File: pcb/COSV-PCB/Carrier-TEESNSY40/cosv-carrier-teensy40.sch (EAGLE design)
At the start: 21 parts, among them K1 61200821621, K2 61200821621, K3 61200821621

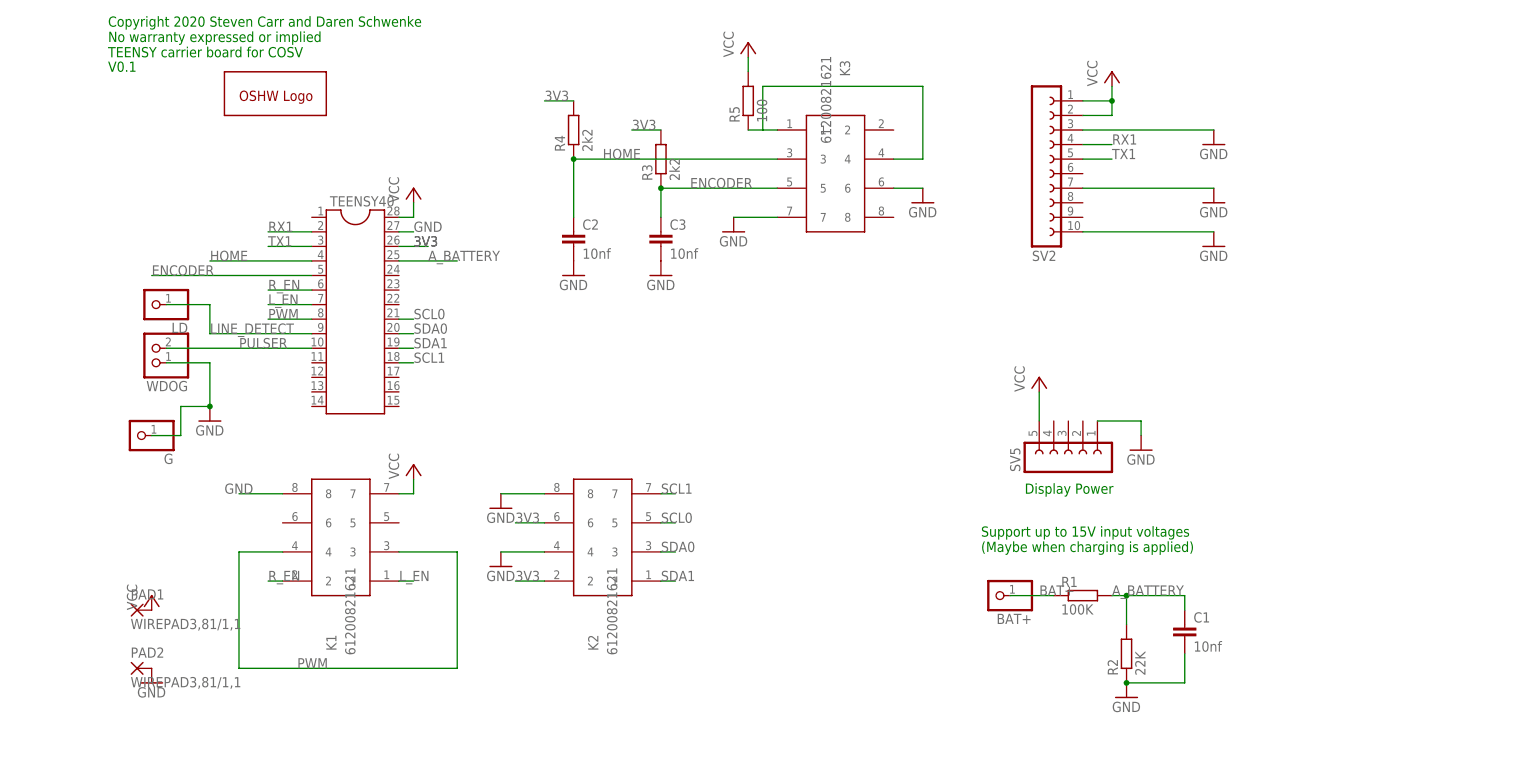
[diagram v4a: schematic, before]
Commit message: Update millable COSV carrier PCB to support milling with a dremel spindle This adds a few more jumpers, but it eliminates the tiny traces between pins that plague milling a board with a dremel spindle.
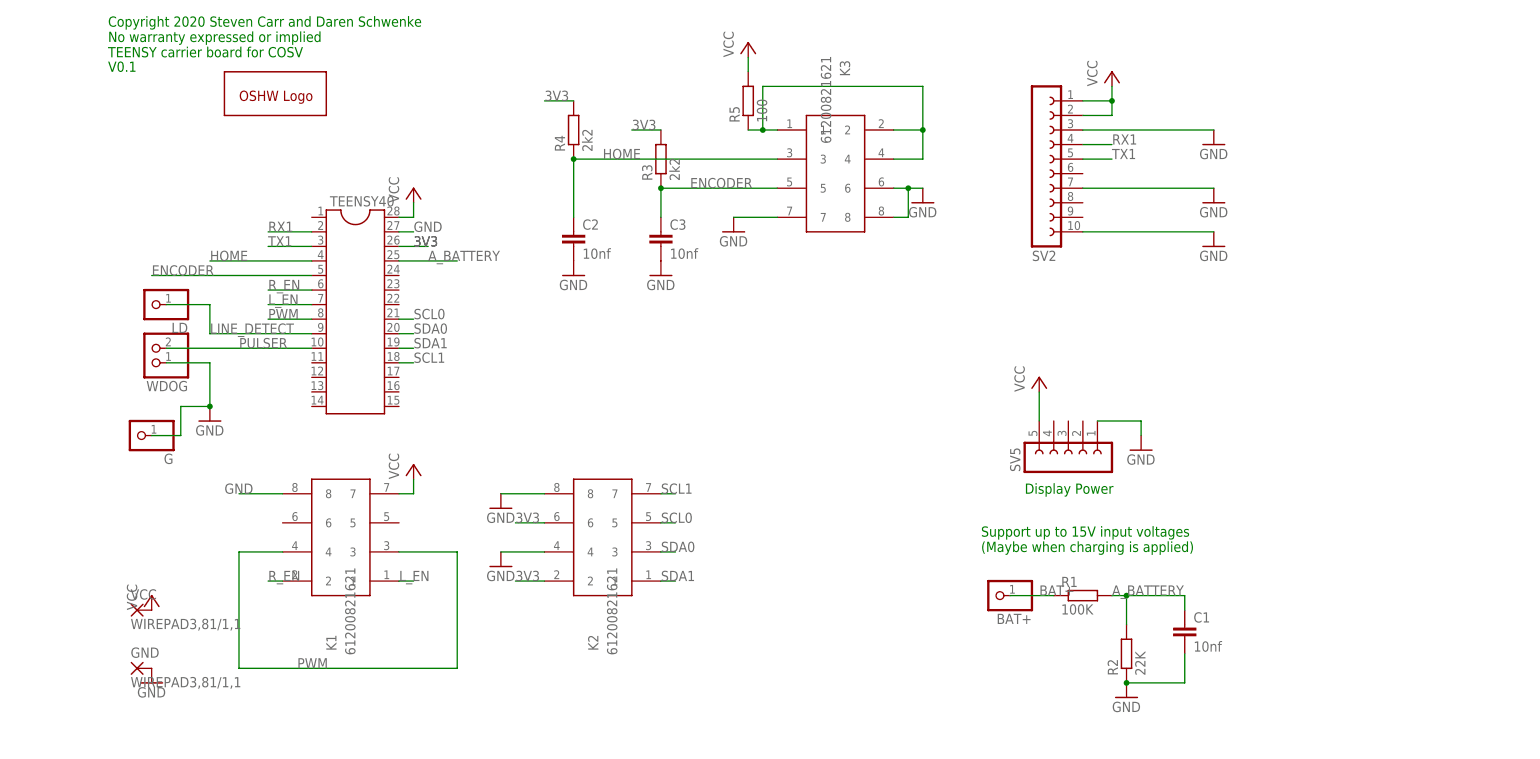
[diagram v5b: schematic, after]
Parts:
- renumbered PAD1 to VCC, PAD2 to GND
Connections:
- net GND: now also K3.8
- net N$1: now also K3.2
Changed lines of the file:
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@@
 <part name="GND3" library="supply1" deviceset="GND" device=""/>
 <part name="K3" library="Wuerth_Elektronik_eiCan_05_Box_Header_IDC_Connectors_1_2" deviceset="61200821621" device=""/>
-<part name="PAD1" library="wirepad" deviceset="WIREPAD" device="3,81/1,1"/>
-<part name="PAD2" library="wirepad" deviceset="WIREPAD" device="3,81/1,1"/>
+<part name="VCC" library="wirepad" deviceset="WIREPAD" device="3,81/1,1"/>
+<part name="GND" library="wirepad" deviceset="WIREPAD" device="3,81/1,1"/>
 <part name="P+1" library="supply1" deviceset="VCC" device=""/>
 <part name="GND1" library="supply1" deviceset="GND" device=""/>
@@
 <instance part="GND3" gate="1" x="71.12" y="25.4"/>
 <instance part="K3" gate="G$1" x="129.54" y="96.52" rot="R270"/>
-<instance part="PAD1" gate="G$1" x="7.62" y="17.78"/>
-<instance part="PAD2" gate="G$1" x="7.62" y="7.62"/>
+<instance part="VCC" gate="G$1" x="7.62" y="17.78"/>
+<instance part="GND" gate="G$1" x="7.62" y="7.62"/>
 <instance part="P+1" gate="VCC" x="10.16" y="20.32"/>
 <instance part="GND1" gate="1" x="10.16" y="5.08"/>
@@
 </segment>
 <segment>
-<pinref part="PAD1" gate="G$1" pin="P"/>
+<pinref part="VCC" gate="G$1" pin="P"/>
 <pinref part="P+1" gate="VCC" pin="VCC"/>
 </segment>
@@
 </segment>
 <segment>
-<pinref part="PAD2" gate="G$1" pin="P"/>
+<pinref part="GND" gate="G$1" pin="P"/>
 <pinref part="GND1" gate="1" pin="GND"/>
 </segment>
@@
 <pinref part="K3" gate="G$1" pin="6"/>
 <pinref part="GND5" gate="1" pin="GND"/>
-<wire x1="139.7" y1="91.44" x2="144.78" y2="91.44" width="0.1524" layer="91"/>
+<wire x1="139.7" y1="91.44" x2="142.24" y2="91.44" width="0.1524" layer="91"/>
+<pinref part="K3" gate="G$1" pin="8"/>
+<wire x1="142.24" y1="91.44" x2="144.78" y2="91.44" width="0.1524" layer="91"/>
+<wire x1="139.7" y1="86.36" x2="142.24" y2="86.36" width="0.1524" layer="91"/>
+<wire x1="142.24" y1="86.36" x2="142.24" y2="91.44" width="0.1524" layer="91"/>
+<junction x="142.24" y="91.44"/>
 </segment>
 </net>
@@
 <pinref part="K3" gate="G$1" pin="4"/>
 <wire x1="139.7" y1="96.52" x2="144.78" y2="96.52" width="0.1524" layer="91"/>
-<wire x1="144.78" y1="96.52" x2="144.78" y2="109.22" width="0.1524" layer="91"/>
-</segment>
-</net>
+<wire x1="144.78" y1="96.52" x2="144.78" y2="101.6" width="0.1524" layer="91"/>
+<pinref part="K3" gate="G$1" pin="2"/>
+<wire x1="144.78" y1="101.6" x2="144.78" y2="109.22" width="0.1524" layer="91"/>
+<wire x1="139.7" y1="101.6" x2="144.78" y2="101.6" width="0.1524" layer="91"/>
+<junction x="144.78" y="101.6"/>
+<junction x="116.84" y="101.6"/>
+</segment>
+</net>
